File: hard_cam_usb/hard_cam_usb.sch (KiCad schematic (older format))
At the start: 2 parts

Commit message: Fixing the last commit
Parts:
- gave numbers to parts that had none: 2
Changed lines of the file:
@@
 $EndDescr
 $Comp
-L 59453-051110ECHLF:59453-051110ECHLF J?
+L 59453-051110ECHLF:59453-051110ECHLF J1
 U 1 1 616991E7
 P 3150 2600
-F 0 "J?" H 3550 2865 50  0000 C CNN
+F 0 "J1" H 3550 2865 50  0000 C CNN
 F 1 "FFC-FPC Conn" H 3550 2774 50  0000 C CNN
 F 2 "59453-051110ECHLF:59453051110ECHLF" H 3800 2700 50  0001 L CNN
@@
 $EndComp
 $Comp
-L power:GND #PWR?
+L power:GND #PWR0101
 U 1 1 61699DE7
 P 3050 2800
-F 0 "#PWR?" H 3050 2550 50  0001 C CNN
+F 0 "#PWR0101" H 3050 2550 50  0001 C CNN
 F 1 "GND" H 3055 2627 50  0000 C CNN
 F 2 "" H 3050 2800 50  0001 C CNN
@@
 Connection ~ 3050 2700
 $Comp
-L power:GND #PWR?
+L power:GND #PWR0102
 U 1 1 6169A6EE
 P 4150 3150
-F 0 "#PWR?" H 4150 2900 50  0001 C CNN
+F 0 "#PWR0102" H 4150 2900 50  0001 C CNN
 F 1 "GND" H 4155 2977 50  0000 C CNN
 F 2 "" H 4150 3150 50  0001 C CNN
@@
 	3950 3000 4100 3000
 $Comp
-L power:VCC #PWR?
+L power:VCC #PWR0103
 U 1 1 6169B282
 P 4100 2400
-F 0 "#PWR?" H 4100 2250 50  0001 C CNN
+F 0 "#PWR0103" H 4100 2250 50  0001 C CNN
 F 1 "VCC" H 4115 2573 50  0000 C CNN
 F 2 "" H 4100 2400 50  0001 C CNN
@@
 D-
 $Comp
-L Connector:USB_B_Mini J?
+L Connector:USB_B_Mini J2
 U 1 1 6169C090
 P 5400 2800
-F 0 "J?" H 5170 2789 50  0000 R CNN
+F 0 "J2" H 5170 2789 50  0000 R CNN
 F 1 "USB_B_Mini" H 5170 2698 50  0000 R CNN
 F 2 "Connector_USB:USB_Mini-B_Wuerth_65100516121_Horizontal" H 5550 2750 50  0001 C CNN
@@
 	3950 2700 4900 2700
 $Comp
-L power:VCC #PWR?
+L power:VCC #PWR0104
 U 1 1 6169DDF0
 P 5000 2450
-F 0 "#PWR?" H 5000 2300 50  0001 C CNN
+F 0 "#PWR0104" H 5000 2300 50  0001 C CNN
 F 1 "VCC" H 5015 2623 50  0000 C CNN
 F 2 "" H 5000 2450 50  0001 C CNN
@@
 	5000 2600 5100 2600
 $Comp
-L power:GND #PWR?
+L power:GND #PWR0105
 U 1 1 6169E390
 P 5450 3350
-F 0 "#PWR?" H 5450 3100 50  0001 C CNN
+F 0 "#PWR0105" H 5450 3100 50  0001 C CNN
 F 1 "GND" H 5455 3177 50  0000 C CNN
 F 2 "" H 5450 3350 50  0001 C CNN

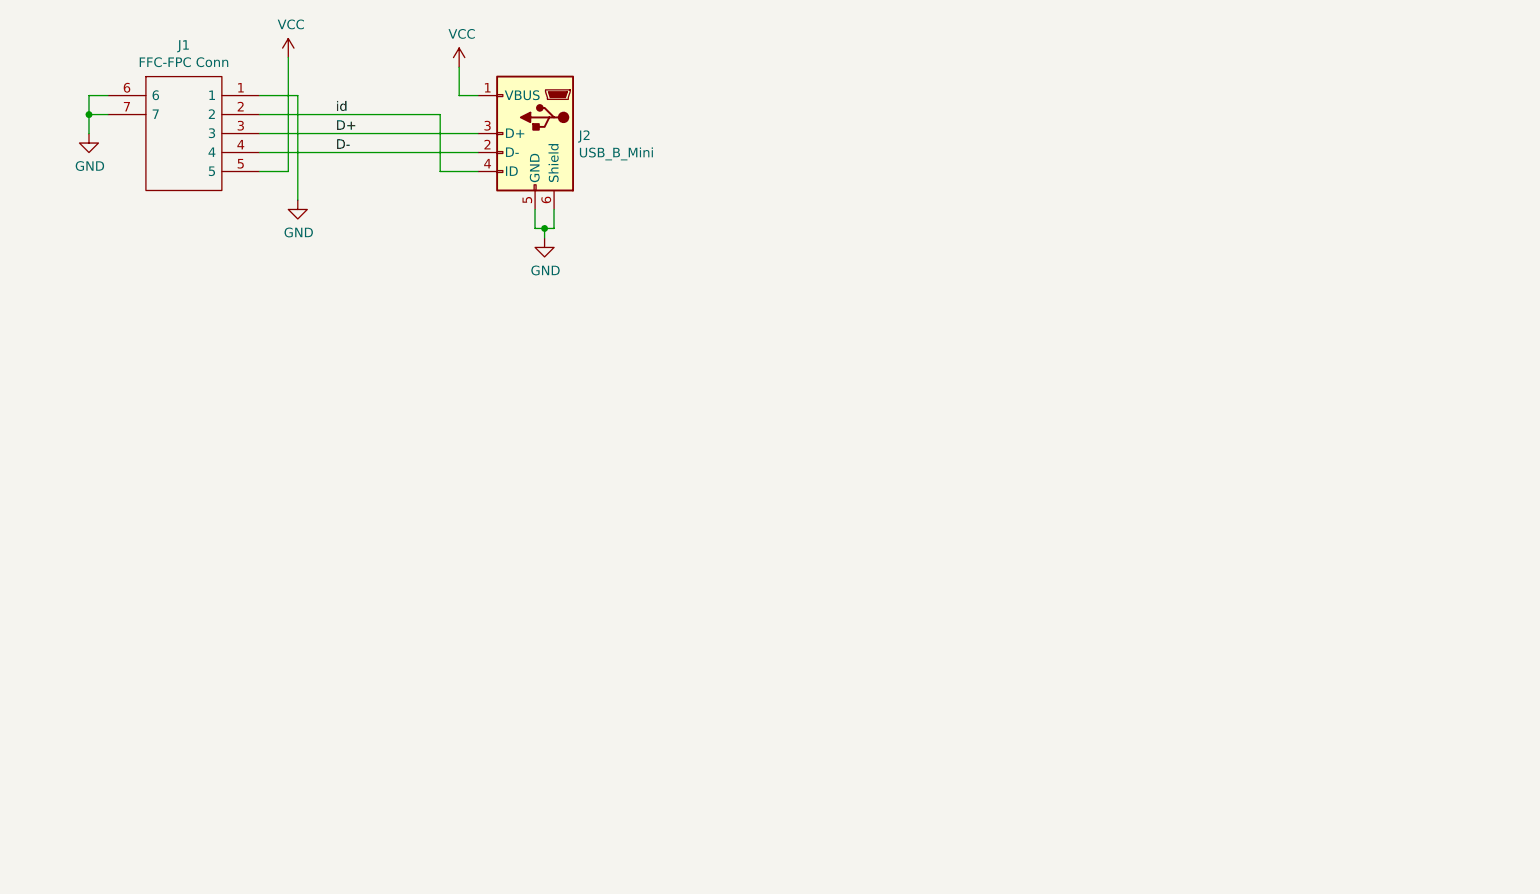
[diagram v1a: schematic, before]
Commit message: sent to production
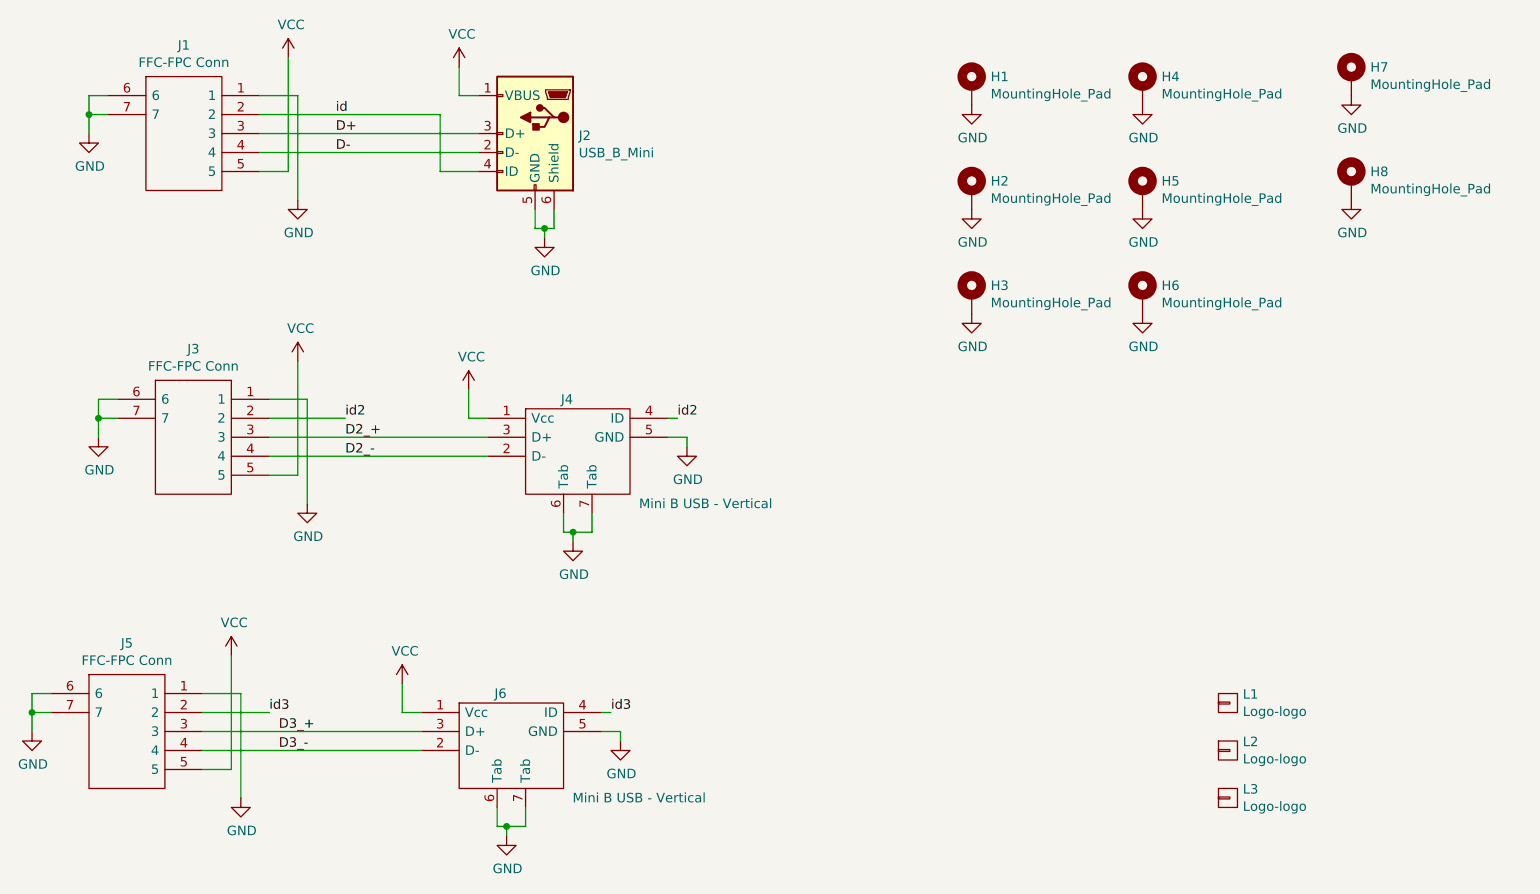
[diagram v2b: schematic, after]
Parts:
- added H1, H2, H3, H4, H5, H6, H7, H8: MountingHole_Pad, MountingHole:MountingHole_3.2mm_M3_Pad_Via, symbol Mechanical:MountingHole_Pad
- added J3, J5: FFC-FPC Conn, 59453-051110ECHLF:59453051110ECHLF, symbol 59453-051110ECHLF:59453-051110ECHLF
- added J4, J6: Mini B USB - Vertical, Hard_PLM:MUSB-B5-S-VT-TSMT-TR, symbol usb_conn:651005136421-651005136421
- added L1, L2, L3: Logo-logo, LED_driver_PCB:logo_vulcur, symbol logo-logo:Logo-logo
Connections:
- net GND: now also H1.1, H2.1, H3.1, H4.1, H5.1, H6.1, H7.1, H8.1, J3.1, J3.6, J3.7, J4.5 (GND), J4.6 (Tab), J4.7 (Tab), J5.1, J5.6, J5.7, J6.5 (GND), J6.6 (Tab), J6.7 (Tab)
- net VCC: now also J3.5, J4.1 (Vcc), J5.5, J6.1 (Vcc)
- new net D2_+: J3.3, J4.3 (D+)
- new net D2_-: J3.4, J4.2 (D-)
- new net D3_+: J5.3, J6.3 (D+)
- new net D3_-: J5.4, J6.2 (D-)
- new net id2: J3.2, J4.4 (ID)
- new net id3: J5.2, J6.4 (ID)
